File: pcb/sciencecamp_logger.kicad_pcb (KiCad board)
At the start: 2 copper layers, 97 x 46 mm, 29 parts, among them J1 1-Wire, J2 HC-SR04, J3 OLED, J4 Micro_SD_Card_Det, SW1 OFF/ON, SW2 action, U1 74LVC125, U2 AMS1117-3.3

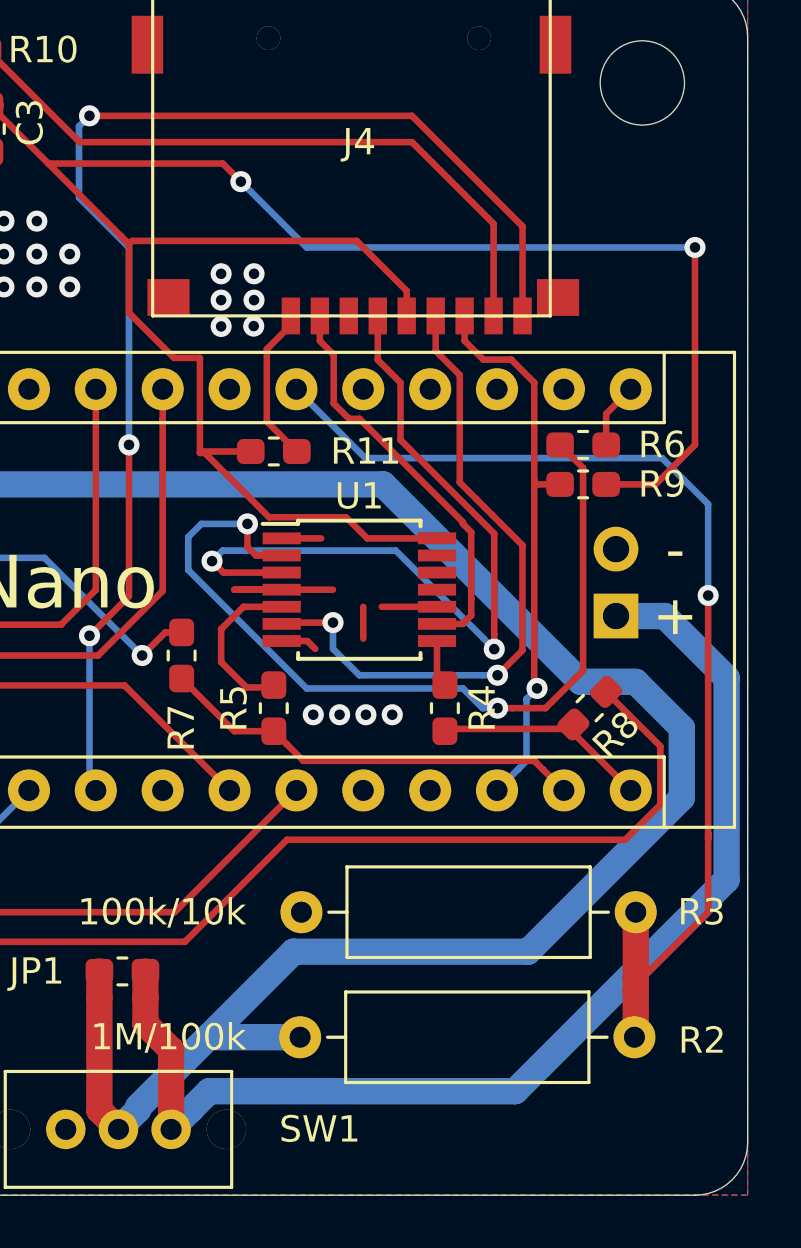
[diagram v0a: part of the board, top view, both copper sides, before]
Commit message: UPD: More GND-surface for bat minus
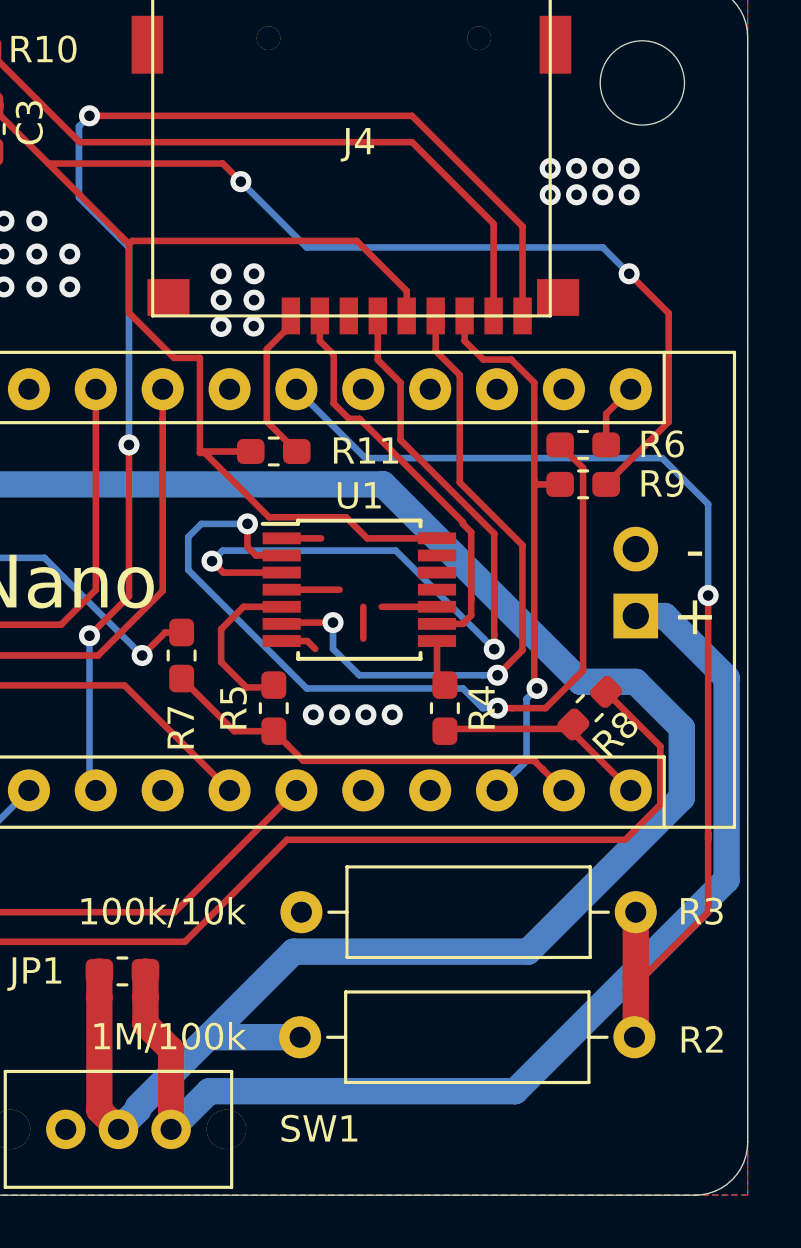
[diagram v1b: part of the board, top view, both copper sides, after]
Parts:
- moved BT1 0.75 mm to (204.8, 100.0)
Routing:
- net SD_3V3: track 99.8 -> 95.6 mm
- net GND: track 11.8 -> 8.41 mm, vias 34 -> 42
- net Net-(BT1-Pad1): track 44.3 -> 43.5 mm
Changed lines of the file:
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@@
     (thickness 1.6)
     (drawings 27)
-    (tracks 314)
+    (tracks 321)
     (zones 0)
     (modules 29)
@@
   )
   (module Connector_PinHeader_2.54mm:PinHeader_1x02_P2.54mm_Vertical (layer B.Cu)
-    (at 204 100)
+    (at 204.75 100)
     (descr "Through hole straight pin header, 1x02, 2.54mm pitch, single row")
     (tags "Through hole pin header THT 1x02 2.54mm single row")
@@
     (effects (font (size 1 1) (thickness 0.15)))
   )
-  (gr_text - (at 206.25 97.5) (layer B.SilkS)
+  (gr_text - (at 207 97.5) (layer B.SilkS)
     (effects (font (size 1.5 1.5) (thickness 0.3)) (justify mirror))
   )
-  (gr_text - (at 206.25 97.5) (layer F.SilkS)
+  (gr_text - (at 207 97.5) (layer F.SilkS)
     (effects (font (size 1.5 1.5) (thickness 0.3)))
   )
-  (gr_text + (at 206.25 100) (layer B.SilkS)
+  (gr_text + (at 207 100) (layer B.SilkS)
     (effects (font (size 1.5 1.5) (thickness 0.3)) (justify mirror))
   )
-  (gr_text + (at 206.25 100) (layer F.SilkS)
+  (gr_text + (at 207 100) (layer F.SilkS)
     (effects (font (size 1.5 1.5) (thickness 0.3)))
   )
@@
   (via (at 177 85) (size 0.8) (drill 0.4) (layers F.Cu B.Cu) (net 2))
   (via (at 177 83.75) (size 0.8) (drill 0.4) (layers F.Cu B.Cu) (net 2))
-  (segment (start 191.3 99) (end 189.5 99) (width 0.25) (layer F.Cu) (net 2))
-  (segment (start 189.5 99) (end 193.25 99) (width 0.25) (layer F.Cu) (net 2))
   (segment (start 197.2 99.65) (end 195.1 99.65) (width 0.25) (layer F.Cu) (net 2))
   (segment (start 191.3 97.05) (end 192.8 97.05) (width 0.25) (layer F.Cu) (net 2))
@@
   (via (at 194.5 103.75) (size 0.8) (drill 0.4) (layers F.Cu B.Cu) (net 2))
   (via (at 195.5 103.75) (size 0.8) (drill 0.4) (layers F.Cu B.Cu) (net 2))
+  (segment (start 191.3 99) (end 193.5 99) (width 0.25) (layer F.Cu) (net 2))
+  (via (at 204.5 84) (size 0.8) (drill 0.4) (layers F.Cu B.Cu) (net 2))
+  (via (at 203.5 84) (size 0.8) (drill 0.4) (layers F.Cu B.Cu) (net 2))
+  (via (at 202.5 84) (size 0.8) (drill 0.4) (layers F.Cu B.Cu) (net 2))
+  (via (at 201.5 84) (size 0.8) (drill 0.4) (layers F.Cu B.Cu) (net 2))
+  (via (at 201.5 83) (size 0.8) (drill 0.4) (layers F.Cu B.Cu) (net 2))
+  (via (at 202.5 83) (size 0.8) (drill 0.4) (layers F.Cu B.Cu) (net 2))
+  (via (at 203.5 83) (size 0.8) (drill 0.4) (layers F.Cu B.Cu) (net 2))
+  (via (at 204.5 83) (size 0.8) (drill 0.4) (layers F.Cu B.Cu) (net 2))
   (segment (start 160 97.79) (end 131.96 97.79) (width 1) (layer B.Cu) (net 5))
   (segment (start 126.75 103) (end 117.75 103) (width 1) (layer B.Cu) (net 5))
@@
   (segment (start 187.1 116.475) (end 186.125 115.5) (width 1) (layer F.Cu) (net 24))
   (segment (start 187.1 119.5) (end 187.1 116.475) (width 1) (layer F.Cu) (net 24))
-  (segment (start 204 100) (end 205.85 100) (width 1) (layer B.Cu) (net 24))
-  (segment (start 187.849999 118.750001) (end 187.1 119.5) (width 1) (layer B.Cu) (net 24))
-  (segment (start 188.550001 118.049999) (end 187.849999 118.750001) (width 1) (layer B.Cu) (net 24))
-  (segment (start 208.200009 110.019993) (end 200.170003 118.049999) (width 1) (layer B.Cu) (net 24))
-  (segment (start 200.170003 118.049999) (end 188.550001 118.049999) (width 1) (layer B.Cu) (net 24))
-  (segment (start 208.200009 102.350009) (end 208.200009 110.019993) (width 1) (layer B.Cu) (net 24))
-  (segment (start 205.85 100) (end 208.200009 102.350009) (width 1) (layer B.Cu) (net 24))
   (segment (start 186.125 115.5) (end 186.125 114.5) (width 1) (layer F.Cu) (net 24))
   (segment (start 186.125 114.5) (end 186.125 113.5) (width 1) (layer F.Cu) (net 24))
+  (segment (start 205.85 100) (end 204.75 100) (width 1) (layer B.Cu) (net 24))
+  (segment (start 208.200009 102.350009) (end 205.85 100) (width 1) (layer B.Cu) (net 24))
+  (segment (start 208.200009 110.019993) (end 208.200009 102.350009) (width 1) (layer B.Cu) (net 24))
+  (segment (start 200.170003 118.049999) (end 208.200009 110.019993) (width 1) (layer B.Cu) (net 24))
+  (segment (start 187.1 119.5) (end 188.550001 118.049999) (width 1) (layer B.Cu) (net 24))
+  (segment (start 188.550001 118.049999) (end 200.170003 118.049999) (width 1) (layer B.Cu) (net 24))
   (segment (start 204.5375 91.4075) (end 204.56 91.385) (width 0.25) (layer F.Cu) (net 26))
   (segment (start 203.625 92.32) (end 204.56 91.385) (width 0.25) (layer F.Cu) (net 26))
@@
   (segment (start 178.375 80.1875) (end 178 80.5625) (width 0.25) (layer F.Cu) (net 29))
   (segment (start 178.375 78.5) (end 178.375 80.1875) (width 0.25) (layer F.Cu) (net 29))
-  (segment (start 203.375 95) (end 205.5 95) (width 0.25) (layer F.Cu) (net 29))
-  (segment (start 205.5 95) (end 207 93.5) (width 0.25) (layer F.Cu) (net 29))
-  (via (at 207 86) (size 0.8) (drill 0.4) (layers F.Cu B.Cu) (net 29))
-  (segment (start 207 93.5) (end 207 86) (width 0.25) (layer F.Cu) (net 29))
   (via (at 189.75 83.5) (size 0.8) (drill 0.4) (layers F.Cu B.Cu) (net 29))
-  (segment (start 207 86) (end 192.25 86) (width 0.25) (layer B.Cu) (net 29))
   (segment (start 192.25 86) (end 189.75 83.5) (width 0.25) (layer B.Cu) (net 29))
   (segment (start 189.0625 82.8125) (end 182.4375 82.8125) (width 0.25) (layer F.Cu) (net 29))
@@
   (segment (start 185.1875 85.5625) (end 182.4375 82.8125) (width 0.25) (layer F.Cu) (net 29))
   (segment (start 182.4375 82.8125) (end 180.25 80.625) (width 0.25) (layer F.Cu) (net 29))
+  (segment (start 203.5 86) (end 192.25 86) (width 0.25) (layer B.Cu) (net 29))
+  (segment (start 204.5 87) (end 203.5 86) (width 0.25) (layer B.Cu) (net 29))
+  (via (at 204.5 87) (size 0.8) (drill 0.4) (layers F.Cu B.Cu) (net 29))
+  (segment (start 203.625 95) (end 206 92.625) (width 0.25) (layer F.Cu) (net 29))
+  (segment (start 206 88.5) (end 204.5 87) (width 0.25) (layer F.Cu) (net 29))
+  (segment (start 206 92.625) (end 206 88.5) (width 0.25) (layer F.Cu) (net 29))
   (segment (start 193.274999 90.074999) (end 192.75 89.55) (width 0.25) (layer F.Cu) (net 30))
   (segment (start 192.75 89.55) (end 192.75 88.6) (width 0.25) (layer F.Cu) (net 30))

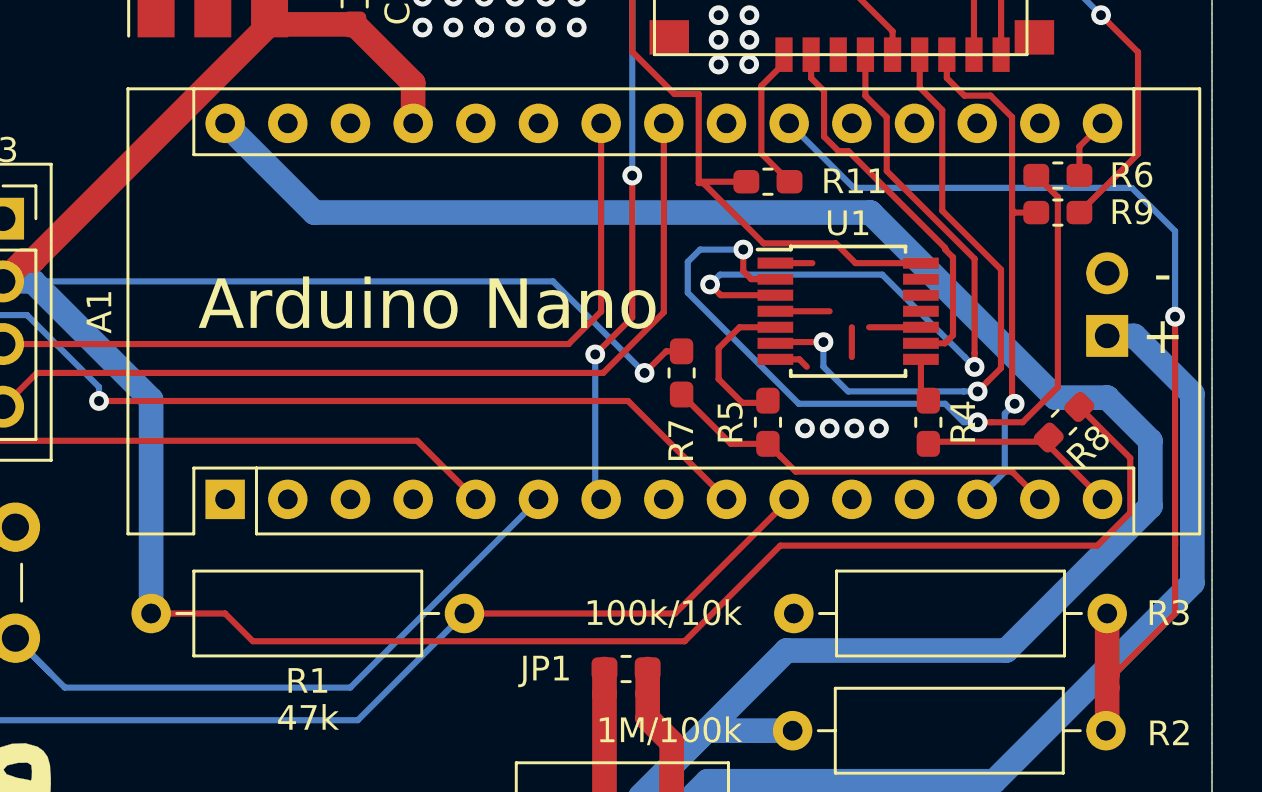
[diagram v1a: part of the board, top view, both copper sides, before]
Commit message: FIX: correct pullup and connected all buffer inputs
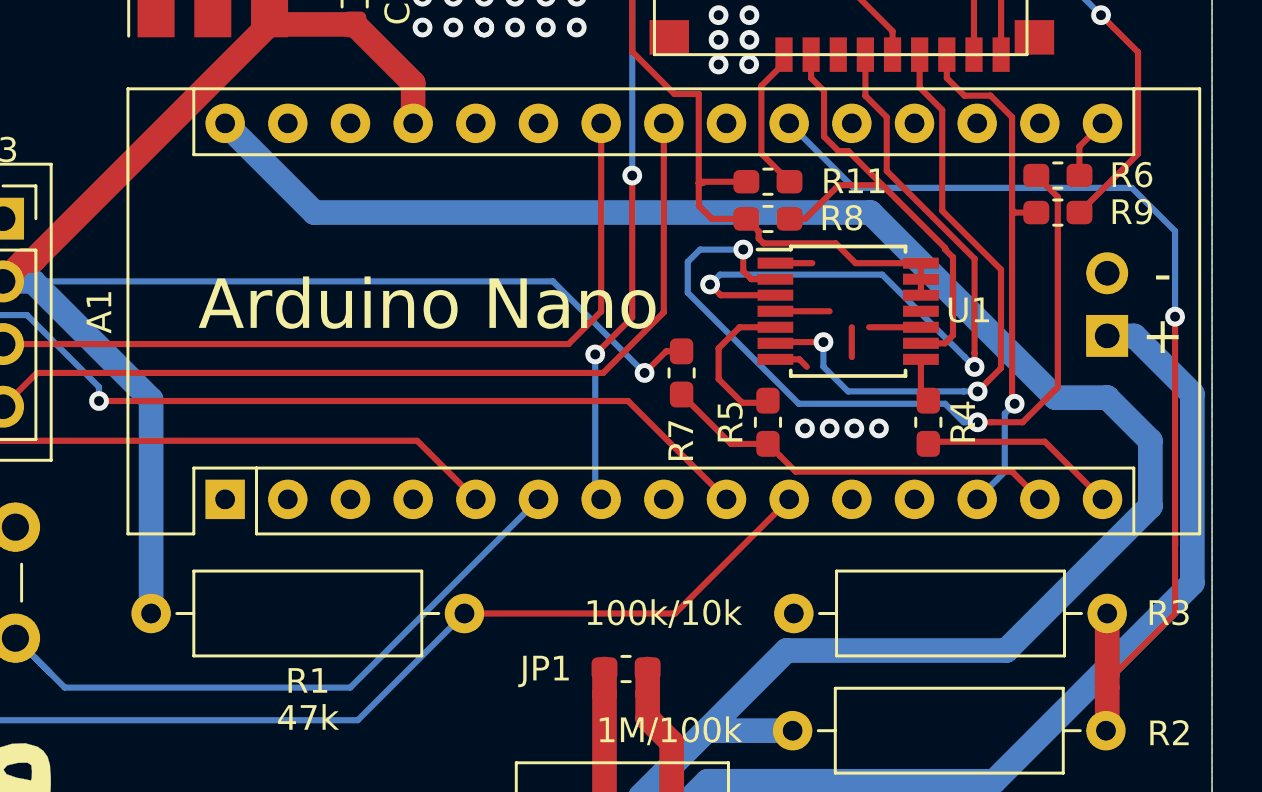
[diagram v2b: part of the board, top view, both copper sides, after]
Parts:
- moved R8 14.6 mm to (191.0, 95.3), turned to 0 degrees
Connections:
- R8 pad 1: +5V -> SD_3V3
- R8 pad 2: MISO -> Net-(J4-Pad7)
- U1 pad 11: (no net) -> Net-(U1-Pad11)
- U1 pad 12: (no net) -> SD_3V3
- U1 pad 13: (no net) -> SD_3V3
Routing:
- net +5V: track 180.8 -> 133.4 mm
- net Net-(J4-Pad7): track 15.4 -> 19.8 mm
- net SD_3V3: track 95.6 -> 97.8 mm
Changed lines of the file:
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@@
     (thickness 1.6)
     (drawings 27)
-    (tracks 321)
+    (tracks 323)
     (zones 0)
     (modules 29)
-    (nets 41)
+    (nets 42)
   )
   (page A4)
@@
   (net 39 SD_SS)
   (net 40 SD_DETECT)
+  (net 41 "Net-(U1-Pad11)")
   (net_class Default "This is the default net class."
     (clearance 0.2)
@@
     (add_net "Net-(R6-Pad1)")
     (add_net "Net-(SW1-Pad1)")
+    (add_net "Net-(U1-Pad11)")
     (add_net SD_3V3)
     (add_net SD_DETECT)
@@
     (tags "SSOP 0.65")
     (attr smd)
-    (fp_text reference U1 (at 0 -3.55) (layer F.SilkS)
+    (fp_text reference U1 (at 4.9 -0.02) (layer F.SilkS)
       (effects (font (size 1 1) (thickness 0.15)))
     )
@@
     (pad 14 smd rect (at 2.95 -1.95) (size 1.45 0.45) (layers F.Cu F.Paste F.Mask)
       (net 29 SD_3V3))
-    (pad 13 smd rect (at 2.95 -1.3) (size 1.45 0.45) (layers F.Cu F.Paste F.Mask))
-    (pad 12 smd rect (at 2.95 -0.65) (size 1.45 0.45) (layers F.Cu F.Paste F.Mask))
-    (pad 11 smd rect (at 2.95 0) (size 1.45 0.45) (layers F.Cu F.Paste F.Mask))
+    (pad 13 smd rect (at 2.95 -1.3) (size 1.45 0.45) (layers F.Cu F.Paste F.Mask)
+      (net 29 SD_3V3))
+    (pad 12 smd rect (at 2.95 -0.65) (size 1.45 0.45) (layers F.Cu F.Paste F.Mask)
+      (net 29 SD_3V3))
+    (pad 11 smd rect (at 2.95 0) (size 1.45 0.45) (layers F.Cu F.Paste F.Mask)
+      (net 41 "Net-(U1-Pad11)"))
     (pad 10 smd rect (at 2.95 0.65) (size 1.45 0.45) (layers F.Cu F.Paste F.Mask)
       (net 2 GND))
@@
   )
   (module Resistor_SMD:R_0603_1608Metric_Pad1.05x0.95mm_HandSolder (layer F.Cu)
-    (at 203 103.5 225)
+    (at 191 95.26)
     (descr "Resistor SMD 0603 (1608 Metric), square (rectangular) end terminal, IPC_7351 nominal with elongated pad for handsoldering. (Body size source: http://www.tortai-tech.com/upload/download/2011102023233369053.pdf), generated with kicad-footprint-generator")
     (tags "resistor handsolder")
     (attr smd)
-    (fp_text reference R8 (at 0 -1.43 45) (layer F.SilkS)
-      (effects (font (size 1 1) (thickness 0.15)))
-    )
-    (fp_text value 47/50k (at 0 1.43 45) (layer F.Fab)
-      (effects (font (size 1 1) (thickness 0.15)))
-    )
-    (fp_text user %R (at 0 0 45) (layer F.Fab)
+    (fp_text reference R8 (at 3 -0.01) (layer F.SilkS)
+      (effects (font (size 1 1) (thickness 0.15)))
+    )
+    (fp_text value 47/50k (at 0 1.43) (layer F.Fab)
+      (effects (font (size 1 1) (thickness 0.15)))
+    )
+    (fp_text user %R (at 0 0) (layer F.Fab)
       (effects (font (size 0.4 0.4) (thickness 0.06)))
     )
@@
     (fp_line (start -0.8 -0.4) (end 0.8 -0.4) (layer F.Fab) (width 0.1))
     (fp_line (start -0.8 0.4) (end -0.8 -0.4) (layer F.Fab) (width 0.1))
-    (pad 2 smd roundrect (at 0.875 0 225) (size 1.05 0.95) (layers F.Cu F.Paste F.Mask) (roundrect_rratio 0.25)
-      (net 27 MISO))
-    (pad 1 smd roundrect (at -0.875 0 225) (size 1.05 0.95) (layers F.Cu F.Paste F.Mask) (roundrect_rratio 0.25)
-      (net 5 +5V))
+    (pad 2 smd roundrect (at 0.875 0) (size 1.05 0.95) (layers F.Cu F.Paste F.Mask) (roundrect_rratio 0.25)
+      (net 30 "Net-(J4-Pad7)"))
+    (pad 1 smd roundrect (at -0.875 0) (size 1.05 0.95) (layers F.Cu F.Paste F.Mask) (roundrect_rratio 0.25)
+      (net 29 SD_3V3))
     (model ${KISYS3DMOD}/Resistor_SMD.3dshapes/R_0603_1608Metric.wrl
       (at (xyz 0 0 0))
@@
   (segment (start 182.29 97.79) (end 160 97.79) (width 0.25) (layer B.Cu) (net 5))
   (segment (start 186 101.5) (end 182.29 97.79) (width 0.25) (layer B.Cu) (net 5))
-  (segment (start 205.685001 107.165001) (end 204.350002 108.5) (width 0.25) (layer F.Cu) (net 5))
-  (segment (start 203.618718 102.881282) (end 205.685001 104.947565) (width 0.25) (layer F.Cu) (net 5))
-  (segment (start 205.685001 104.947565) (end 205.685001 107.165001) (width 0.25) (layer F.Cu) (net 5))
-  (segment (start 204.350002 108.5) (end 191.5 108.5) (width 0.25) (layer F.Cu) (net 5))
-  (segment (start 187.624999 112.375001) (end 170.124999 112.375001) (width 0.25) (layer F.Cu) (net 5))
-  (segment (start 191.5 108.5) (end 187.624999 112.375001) (width 0.25) (layer F.Cu) (net 5))
-  (segment (start 168.999998 111.25) (end 166 111.25) (width 0.25) (layer F.Cu) (net 5))
-  (segment (start 170.124999 112.375001) (end 168.999998 111.25) (width 0.25) (layer F.Cu) (net 5))
   (segment (start 187.235 111.25) (end 191.86 106.625) (width 0.25) (layer F.Cu) (net 8))
   (segment (start 178.7 111.25) (end 187.235 111.25) (width 0.25) (layer F.Cu) (net 8))
@@
   (segment (start 193.75 96.25) (end 190.823002 96.25) (width 0.25) (layer F.Cu) (net 29))
   (segment (start 188.378003 93.805001) (end 188.194999 93.805001) (width 0.25) (layer F.Cu) (net 29))
-  (segment (start 190.823002 96.25) (end 188.378003 93.805001) (width 0.25) (layer F.Cu) (net 29))
   (segment (start 178.375 80.1875) (end 178 80.5625) (width 0.25) (layer F.Cu) (net 29))
   (segment (start 178.375 78.5) (end 178.375 80.1875) (width 0.25) (layer F.Cu) (net 29))
@@
   (segment (start 206 88.5) (end 204.5 87) (width 0.25) (layer F.Cu) (net 29))
   (segment (start 206 92.625) (end 206 88.5) (width 0.25) (layer F.Cu) (net 29))
+  (segment (start 197.2 97.05) (end 197.2 98.35) (width 0.25) (layer F.Cu) (net 29))
+  (segment (start 188.194999 93.805001) (end 188.194999 94.724999) (width 0.25) (layer F.Cu) (net 29))
+  (segment (start 188.73 95.26) (end 190.125 95.26) (width 0.25) (layer F.Cu) (net 29))
+  (segment (start 188.194999 94.724999) (end 188.73 95.26) (width 0.25) (layer F.Cu) (net 29))
+  (segment (start 190.624072 96.05107) (end 190.823002 96.25) (width 0.25) (layer F.Cu) (net 29))
+  (segment (start 190.624072 95.759072) (end 190.624072 96.05107) (width 0.25) (layer F.Cu) (net 29))
+  (segment (start 190.125 95.26) (end 190.624072 95.759072) (width 0.25) (layer F.Cu) (net 29))
   (segment (start 193.274999 90.074999) (end 192.75 89.55) (width 0.25) (layer F.Cu) (net 30))
   (segment (start 192.75 89.55) (end 192.75 88.6) (width 0.25) (layer F.Cu) (net 30))
   (segment (start 193.274999 91.925001) (end 193.274999 90.074999) (width 0.25) (layer F.Cu) (net 30))
-  (segment (start 198.185001 96.435001) (end 194.260001 92.510001) (width 0.25) (layer F.Cu) (net 30))
   (segment (start 198.185001 96.499999) (end 198.185001 96.435001) (width 0.25) (layer F.Cu) (net 30))
   (segment (start 194.260001 92.510001) (end 193.859999 92.510001) (width 0.25) (layer F.Cu) (net 30))
@@
   (segment (start 198.499989 99.975011) (end 198.499989 99.363601) (width 0.25) (layer F.Cu) (net 30))
   (segment (start 198.5 99.36359) (end 198.5 96.814998) (width 0.25) (layer F.Cu) (net 30))
+  (segment (start 193.865 93.895) (end 195.645 93.895) (width 0.25) (layer F.Cu) (net 30))
+  (segment (start 192.5 95.26) (end 193.865 93.895) (width 0.25) (layer F.Cu) (net 30))
+  (segment (start 191.875 95.26) (end 192.5 95.26) (width 0.25) (layer F.Cu) (net 30))
+  (segment (start 198.185001 96.435001) (end 195.645 93.895) (width 0.25) (layer F.Cu) (net 30))
+  (segment (start 195.645 93.895) (end 194.260001 92.510001) (width 0.25) (layer F.Cu) (net 30))
   (via (at 199.5 102.25) (size 0.8) (drill 0.4) (layers F.Cu B.Cu) (net 31))
   (segment (start 199.5 102.25) (end 198.934315 102.25) (width 0.25) (layer B.Cu) (net 31))
